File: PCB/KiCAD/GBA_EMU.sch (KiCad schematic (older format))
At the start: 2 parts

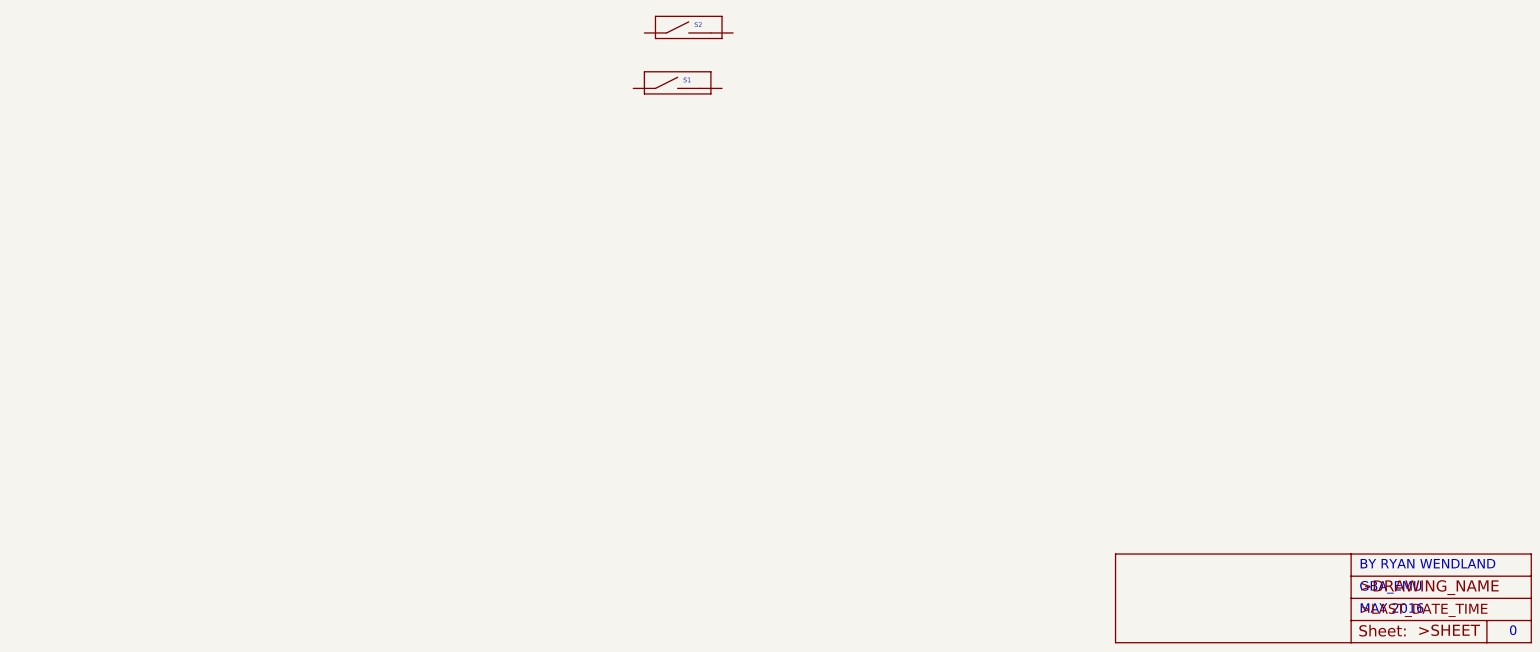
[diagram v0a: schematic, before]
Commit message: imported footprints
button footprints from https://github.com/AEFeinstein/gbaZero
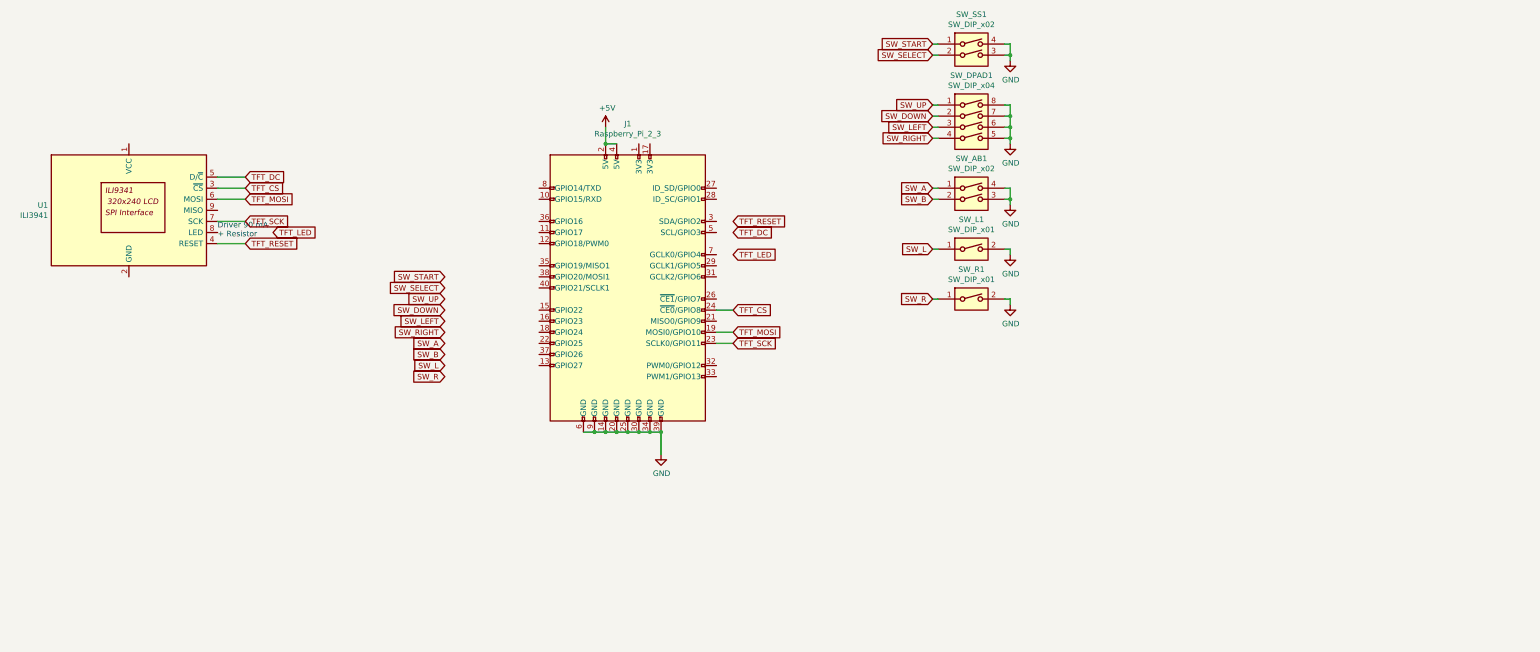
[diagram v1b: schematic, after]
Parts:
- removed S1, S2: SHOULDER_BUTTON, GBA_EMU:SHOULDER_BUTTON, symbol GBA_EMU-eagle-import:SHOULDER_BUTTON
- added J1: Raspberry_Pi_2_3, Module:Raspberry_Pi_Zero_Socketed_THT_FaceDown_MountingHoles, symbol Connector:Raspberry_Pi_2_3
- added SW_AB1: SW_DIP_x02, GBA_EMU:AB_BUTTON, symbol Switch:SW_DIP_x02
- added SW_DPAD1: SW_DIP_x04, GBA_EMU:D-PAD, symbol Switch:SW_DIP_x04
- added SW_L1, SW_R1: SW_DIP_x01, GBA_EMU:SHOULDER_BUTTON, symbol Switch:SW_DIP_x01
- added SW_SS1: SW_DIP_x02, GBA_EMU:START_SELECT_BUTTON, symbol Switch:SW_DIP_x02
- added U1: ILI3941, Display:CR2013-MI2120, symbol GBA_EMU-eagle-import:ILI3941
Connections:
- new net +5V: J1.2 (5V), J1.4 (5V)
- new net GND: J1.14 (GND), J1.20 (GND), J1.25 (GND), J1.30 (GND), J1.34 (GND), J1.39 (GND), J1.6 (GND), J1.9 (GND), SW_AB1.3, SW_AB1.4, SW_DPAD1.5, SW_DPAD1.6, SW_DPAD1.7, SW_DPAD1.8, SW_L1.2, SW_R1.2, SW_SS1.3, SW_SS1.4
- new net SW_A: SW_AB1.1
- new net SW_B: SW_AB1.2
- new net SW_DOWN: SW_DPAD1.2
- new net SW_L: SW_L1.1
- new net SW_LEFT: SW_DPAD1.3
- new net SW_R: SW_R1.1
- new net SW_RIGHT: SW_DPAD1.4
- new net SW_SELECT: SW_SS1.2
- new net SW_START: SW_SS1.1
- new net SW_UP: SW_DPAD1.1
- new net TFT_CS: J1.24 (~CE0~/GPIO8), U1.3 (~CS)
- new net TFT_DC: U1.5 (D/~C)
- new net TFT_MOSI: J1.19 (MOSI0/GPIO10), U1.6 (MOSI)
- new net TFT_RESET: U1.4 (RESET)
- new net TFT_SCK: J1.23 (SCLK0/GPIO11), U1.7 (SCK)
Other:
- note added: "Driver 90 mA\n+ Resistor"
- note removed: "0"
- note removed: "BY RYAN WENDLAND"
- note removed: "GBA_EMU"
- note removed: "MAY 2016"

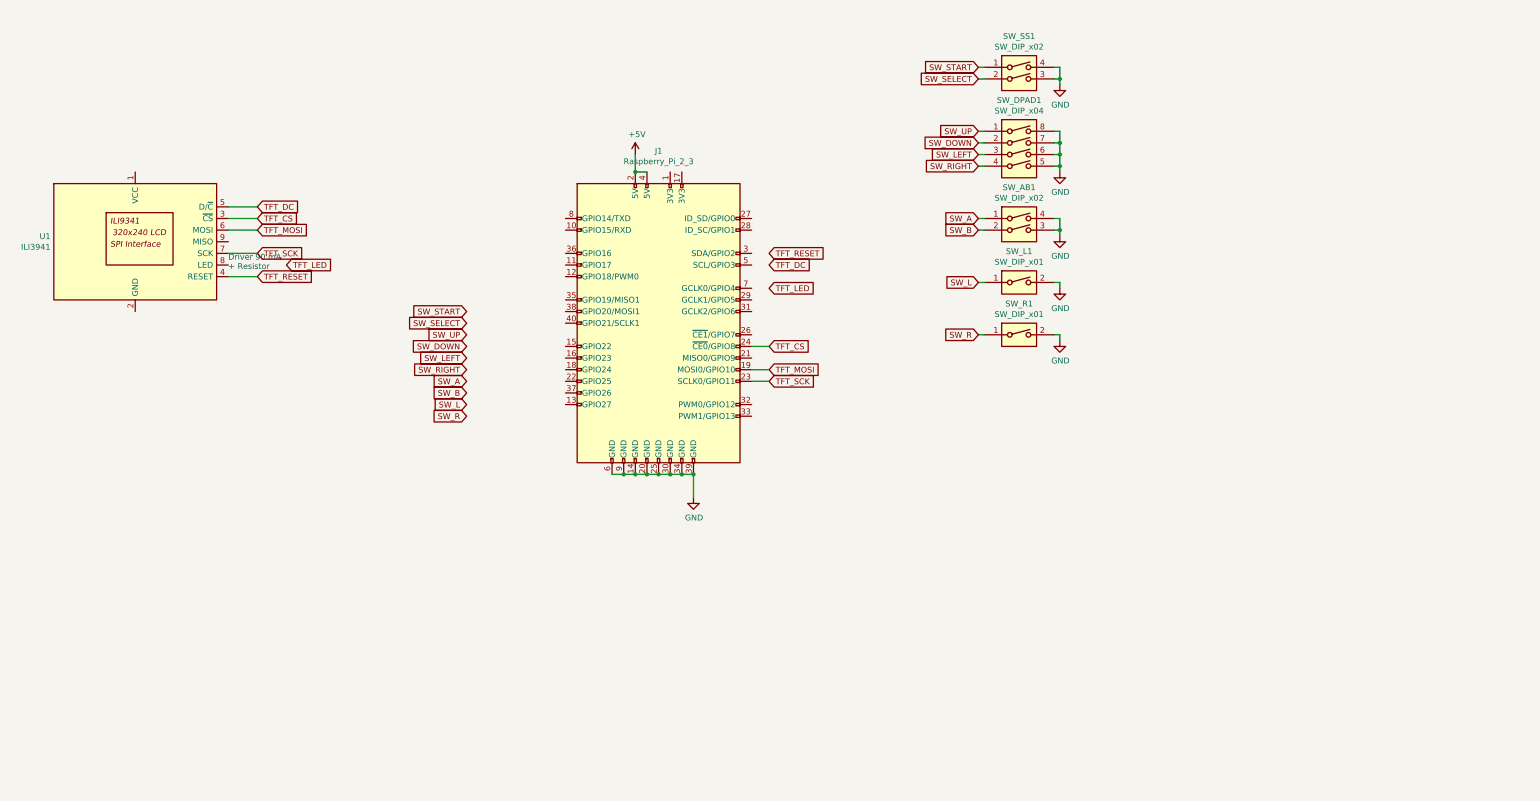
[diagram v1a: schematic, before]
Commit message: LCD Connection
https://github.com/juj/fbcp-ili9341#if-you-wired-the-display-to-the-pi-yourself

https://sudomod.com/forum/viewtopic.php?f=22&t=5854

Screen<------------>Raspberry Pi 3 or zero
LED<-------------->Pin 12 (GPIO18)
SCK<-------------->Pin 23 (GPIO11)
SDI(MOSI)<----->Pin 19 (GPIO10)
DC<--------------->Pin 22 (GPIO24)
RESET<----------->Pin 26 (GPIO25)
CS<----------------->Pin 24 (GPIO8)
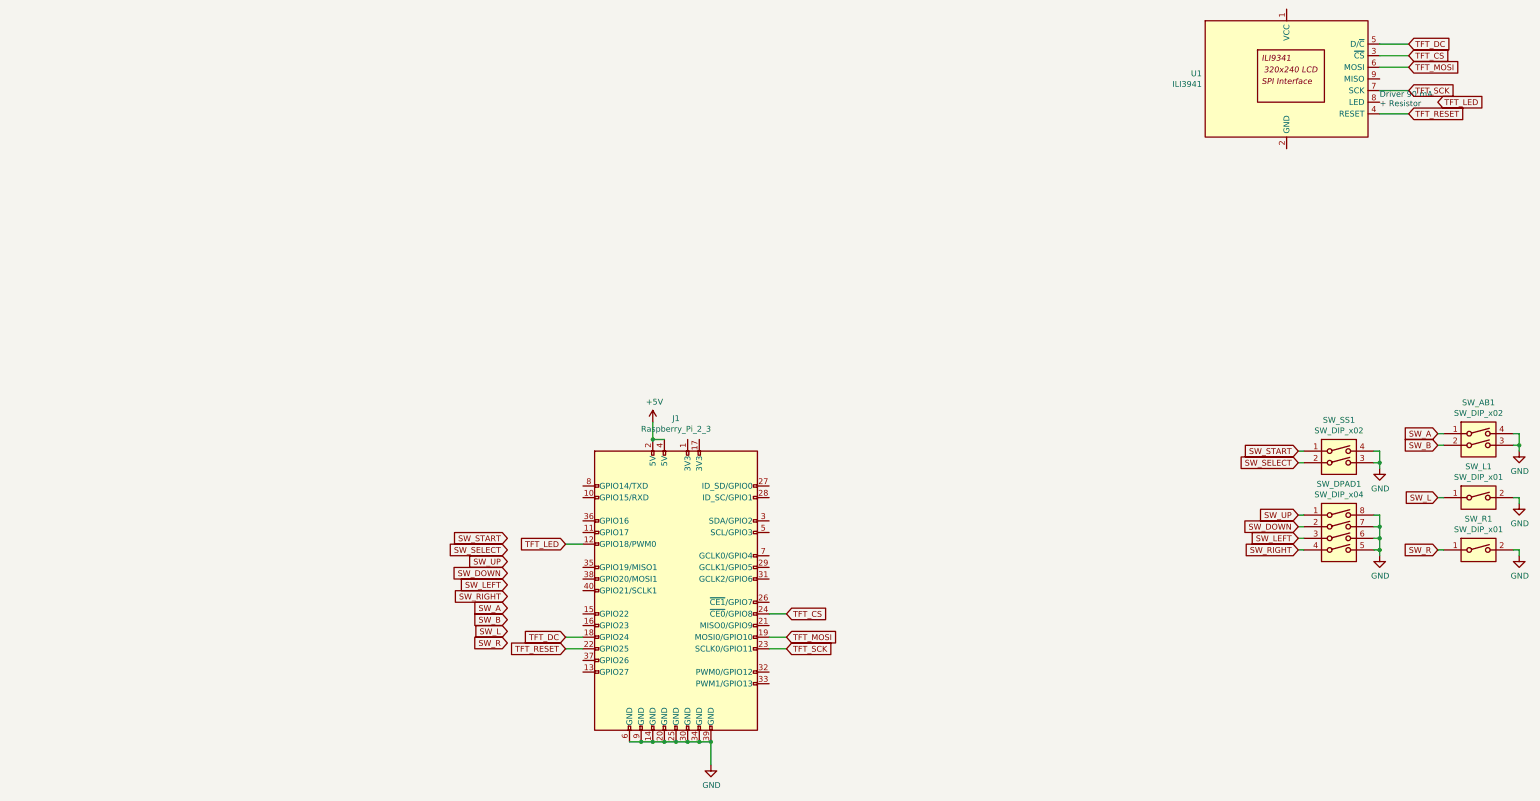
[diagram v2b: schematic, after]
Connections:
- net TFT_DC: now also J1.18 (GPIO24)
- net TFT_LED: now also J1.12 (GPIO18/PWM0)
- net TFT_RESET: now also J1.22 (GPIO25)
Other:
- moved on the sheet: J1, SW_AB1, SW_DPAD1, SW_L1, SW_R1, SW_SS1, U1

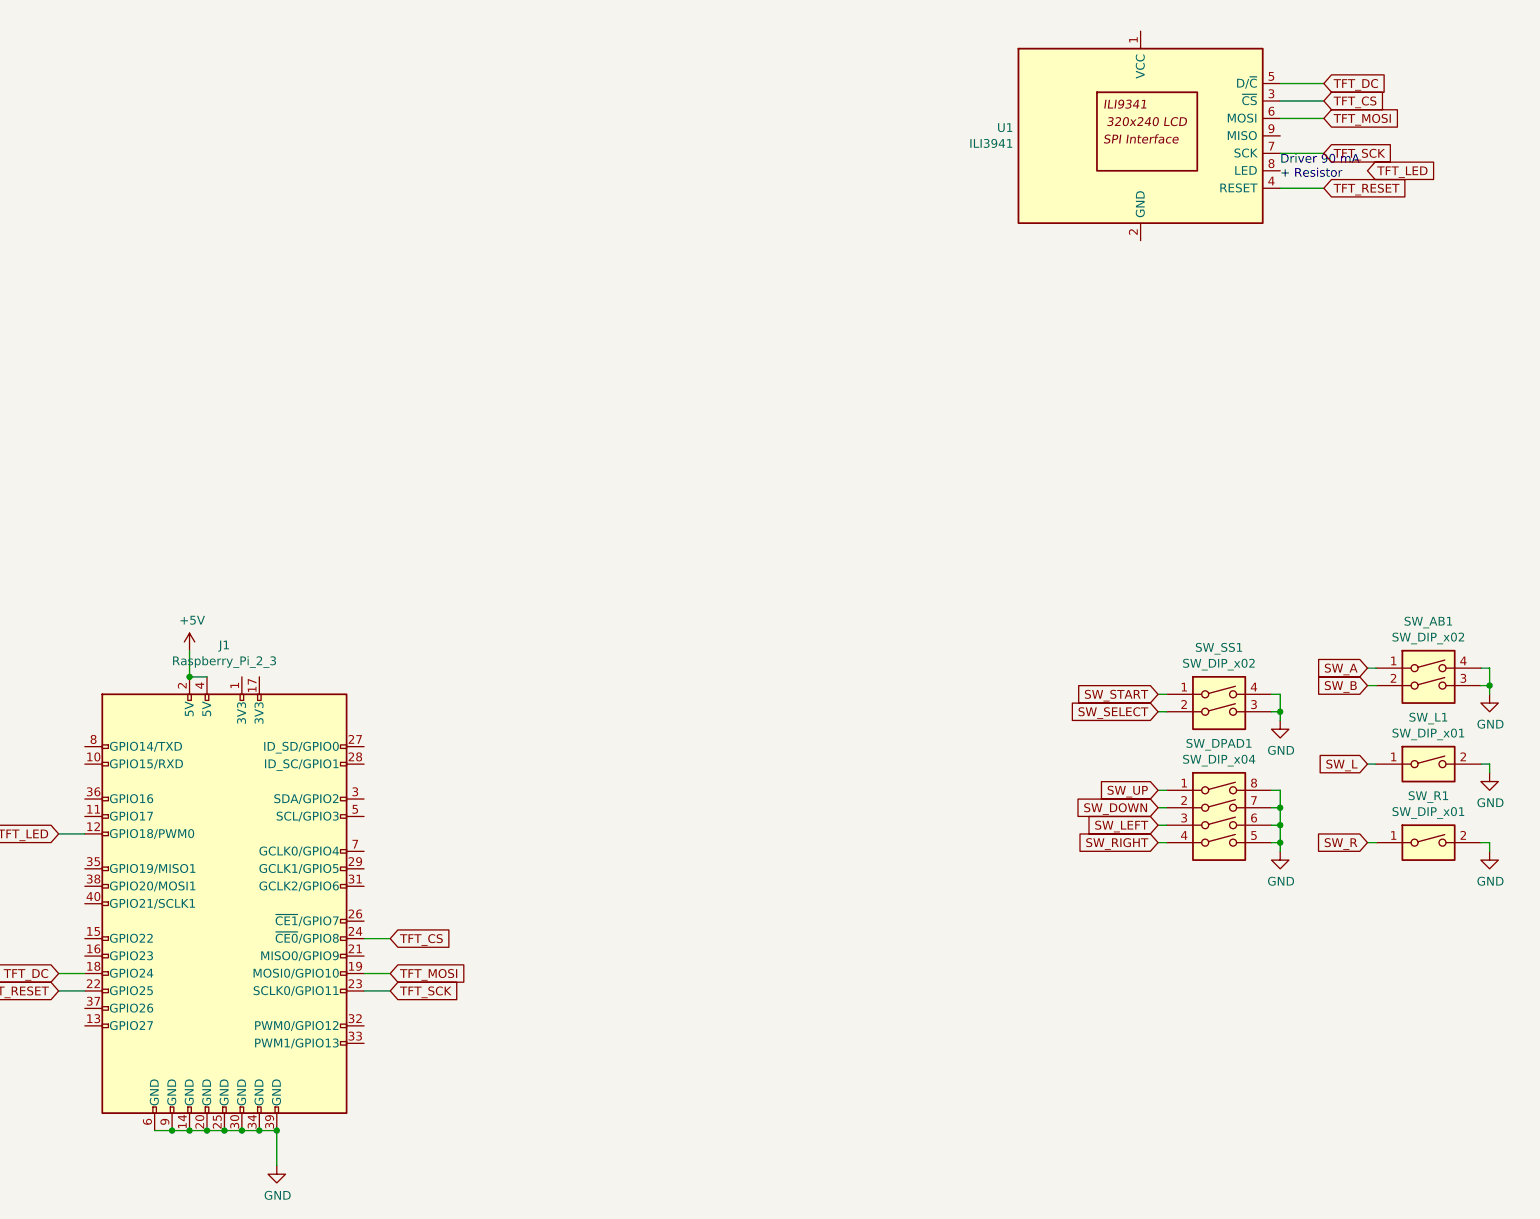
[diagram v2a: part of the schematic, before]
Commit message: PWM Audio
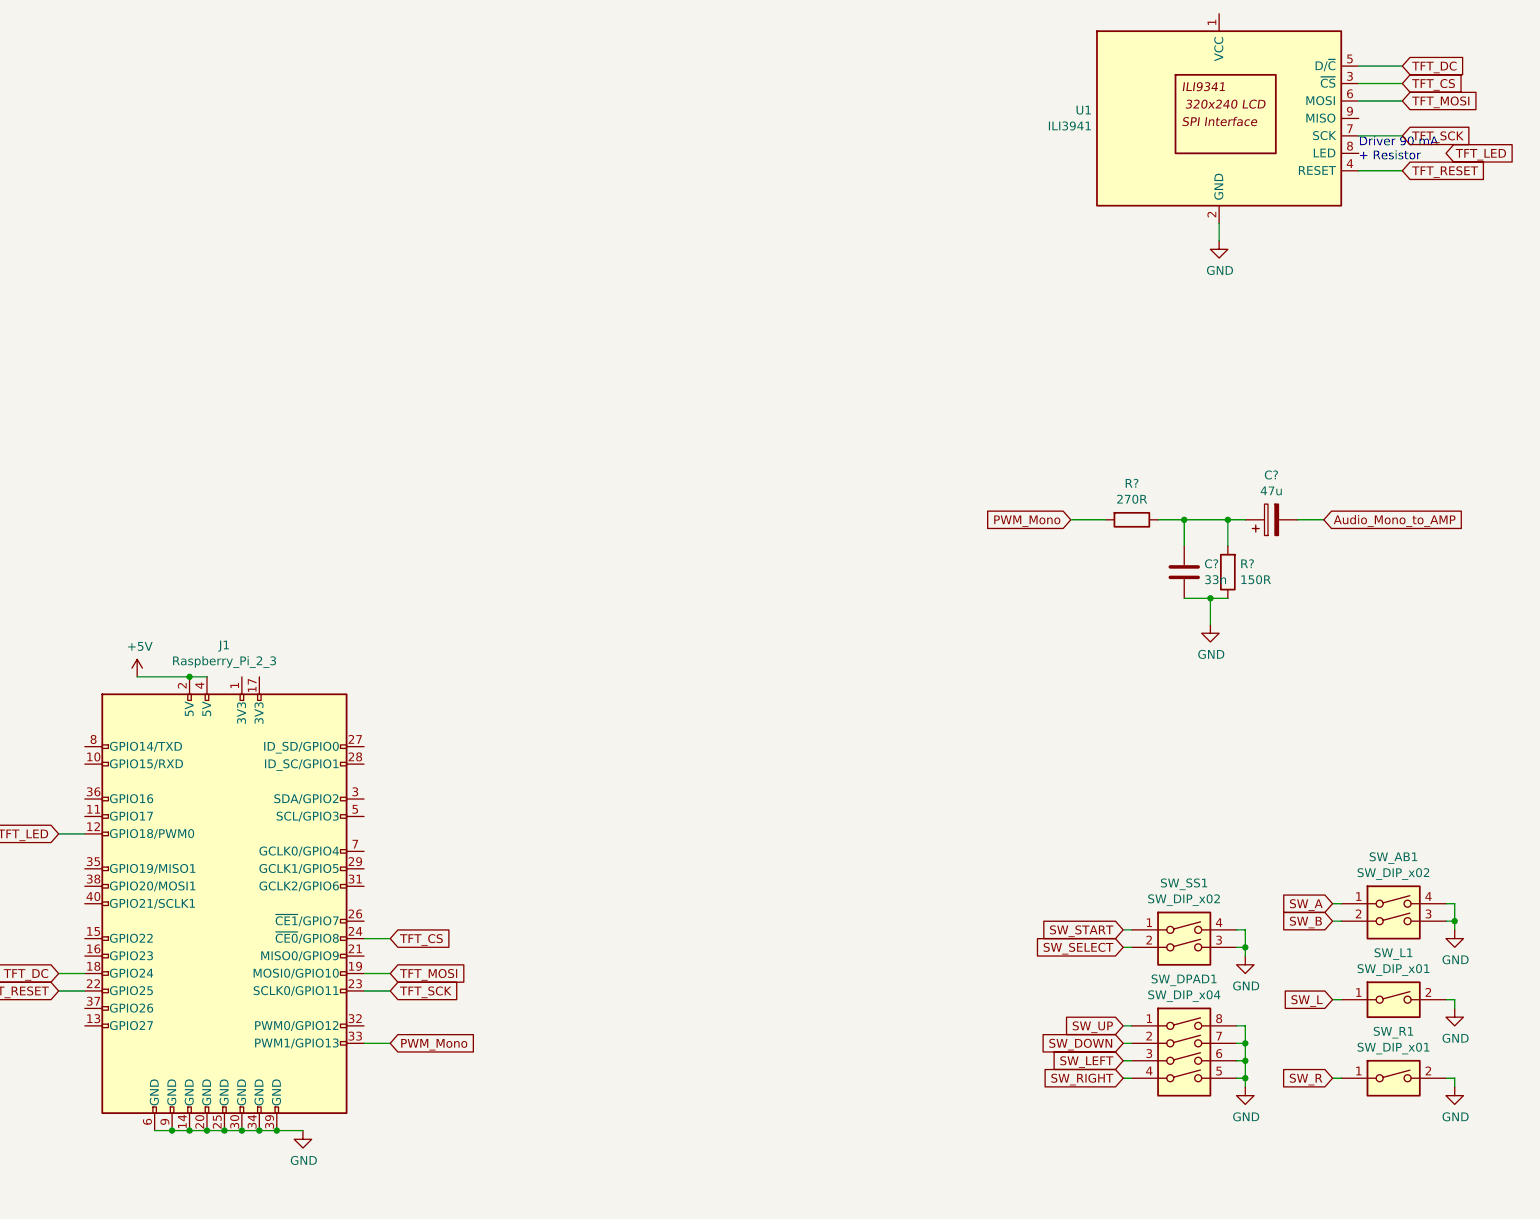
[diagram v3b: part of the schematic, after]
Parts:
- added C?: 33n, symbol Device:C
- added C?: 47u, symbol Device:CP
- added R?: 270R, symbol Device:R
- added R?: 150R, symbol Device:R
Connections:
- net GND: now also U1.2 (GND), C?.2, R?.1
- net PWM_Mono: now reaches J1.33 (PWM1/GPIO13)
- net PWM_Mono: now also R?.2
- new net: C?.1, C?.1, R?.1, R?.2
- new net Audio_Mono_to_AMP: C?.2
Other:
- moved on the sheet: SW_AB1, SW_DPAD1, SW_L1, SW_R1, SW_SS1, U1

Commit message: Audio, LCD, Buttons
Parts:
- removed U1: ILI3941, Display:CR2013-MI2120, symbol GBA_EMU-eagle-import:ILI3941
- added C1: 100n, Capacitor_SMD:C_0805_2012Metric_Pad1.15x1.40mm_HandSolder, symbol Device:C
- added C2: 10u, Capacitor_SMD:C_0805_2012Metric_Pad1.15x1.40mm_HandSolder, symbol Device:C
- added C3, C7: 1u, Capacitor_SMD:CP_Elec_4x5.4, symbol Device:CP
- added C5: 100u, Capacitor_SMD:CP_Elec_5x5.4, symbol Device:CP
- added D1: 1N4148, Diode_SMD:D_MiniMELF, symbol Diode:1N4148
- added LS1: Speaker, Connector_Wire:SolderWirePad_1x02_P3.81mm_Drill0.8mm, symbol Device:Speaker
- added Q1: BSS138, Package_TO_SOT_SMD:SOT-23, symbol Transistor_FET:BSS138
- added R1, R2, R4, R8: 100, Resistor_SMD:R_0805_2012Metric_Pad1.15x1.40mm_HandSolder, symbol Device:R
- added R3: 3.9K, Resistor_SMD:R_0805_2012Metric_Pad1.15x1.40mm_HandSolder, symbol Device:R
- added R7: 150, Resistor_SMD:R_0805_2012Metric_Pad1.15x1.40mm_HandSolder, symbol Device:R
- added R? (x2): 100k, Resistor_SMD:R_0805_2012Metric_Pad1.15x1.40mm_HandSolder, symbol Device:R
- added RV?: 10k, symbol Device:R_POT
- added U1: ILI3941, GBA_EMU:18PIN-0.8MM, symbol GBA_EMU:ILI3941
- added U2: LM4875, Package_SO:SOIC-8_3.9x4.9mm_P1.27mm, symbol GBA_EMU:LM4875
- C4: renamed from C?; footprint (none) -> Capacitor_SMD:CP_Elec_5x5.4
- C6: renamed from C?; footprint (none) -> Capacitor_SMD:C_0805_2012Metric_Pad1.15x1.40mm_HandSolder
- J1: footprint Module:Raspberry_Pi_Zero_Socketed_THT_FaceDown_MountingHoles -> GBA_EMU:Raspberry_Pi_Zero_Socketed_THT_FaceDown_MountingHoles
- R5: renamed from R?; value 270R -> 270; footprint (none) -> Resistor_SMD:R_0805_2012Metric_Pad1.15x1.40mm_HandSolder
- R6: renamed from R?; value 150R -> 150; footprint (none) -> Resistor_SMD:R_0805_2012Metric_Pad1.15x1.40mm_HandSolder
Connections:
- net +5V: now also C1.1, C2.1, C3.1, R?.2, RV?.1, U1.10 (LED_A), U2.1 (VDD)
- net GND: now also C1.2, C2.2, C3.2, C7.2, Q1.2 (S), R7.1, RV?.3, U1.1 (GND), U1.8 (GND), U2.6 (GND)
- net PWM_Mono: now also J1.12 (GPIO18/PWM0); no longer J1.33 (PWM1/GPIO13)
- net TFT_CS: now also U1.5 (~CS)
- net TFT_DC: now also U1.4 (D/~C)
- net TFT_LED: now also J1.33 (PWM1/GPIO13), D1.1 (K); no longer J1.12 (GPIO18/PWM0)
- net TFT_MOSI: now also U1.6 (MOSI)
- net TFT_RESET: now also U1.2 (RESET)
- net TFT_SCK: now also U1.3 (SCK)
- net +3V3: now reaches J1.1 (3V3)
- net +3V3: now also J1.17 (3V3), R3.2, U1.9 (VCC)
- net TFT_MISO: now reaches J1.21 (MISO0/GPIO9)
- net TFT_MISO: now also U1.7 (MISO)
- net Audio_Mono_to_AMP renamed Audio
- net Audio: now also U2.2 (VIN)
- new net: LS1.1, U2.8 (VOUT2)
- new net: C5.1, LS1.2, U2.5 (VOUT1)
- new net: D1.2 (A), Q1.1 (G), R3.1
- new net: Q1.3 (D), R1.2, R2.2, R4.2, R8.2
- new net: R1.1, U1.11 (LED_K1)
- new net: R2.1, U1.12 (LED_K2)
- new net: R4.1, U1.13 (LED_K3)
- new net: R8.1, U1.14 (LED_K4)
- new net: R?.2, U2.3 (HP_Sns)
- new net: RV?.2, U2.4 (VOL)
- new net: C7.1, U2.7 (BYPASS)
- new net HP_OUT: C5.2, R7.2
- new net HP_SNS: R?.1, R?.1
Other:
- note removed: "Driver 90 mA\n+ Resistor"
- moved on the sheet: C4, C6, J1, R5, R6, SW_AB1, SW_DPAD1, SW_L1, SW_R1, SW_SS1
